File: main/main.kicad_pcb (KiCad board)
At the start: 4 copper layers, 94.8 x 88 mm, 101 parts, among them J1 Micro_SD_Card_Det1, J10 STKHEADER_B1_R, J11 STKHEADER_B1_L, J12 STKHEADER_B2_R, J13 SCRTERM_Board3ConnPt, J2 HEADER_ST-Link IN, J4 3.7V_IN, J5 Voltmeter_OUT, J6 SCRTERM_Board3ConnPt, J7 HEADER_ST-Link IN, J8 HEADER_ST-Link IN, J9 STKHEADER_B2_L, U1 STM32F405RGTx, U12 BMI323, U13 MAX-M10S, U2 LSM6DSL, U3 MMC5883MA, U4 AP63203WU, U5 THVD1420D, U7 STM32G071CBT6, U8 STM32G071CBT6, U9 THVD1420D

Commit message: work on dsn checklist
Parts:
- removed C22, C31, C33: 100n, Capacitor_SMD:C_0603_1608Metric
- added Q1: AO3401A, Package_TO_SOT_SMD:SOT-23, F.Cu at (176.9, 53.1)
- added R18: 10k, Resistor_SMD:R_0603_1608Metric, F.Cu at (173.4, 52.3)
- J4: value 3.7V_IN -> 7.4IN
- L1: footprint Inductor_SMD:L_0603_1608Metric -> Inductor_SMD:L_6.3x6.3_H3
- U10, U11, U6: footprint Oscillator:Oscillator_SMD_SCTF_SX3M8.000M20F30TNN -> Crystal:Crystal_SMD_3225-4Pin_3.2x2.5mm
- U5, U9: value THVD1420D -> SP3485EN
- moved L1 4.14 mm to (173.8, 63.0)
- moved R14 2.19 mm to (192.7, 116.3), turned to 90 degrees
- moved D1 1.86 mm to (173.3, 83.3)
- moved R8 1.80 mm to (171.6, 83.3), turned to -90 degrees
- moved D2 1.44 mm to (190.9, 116.3)
- moved U10 1.10 mm to (131.6, 127.6), turned to 180 degrees
- moved U6 0.36 mm to (178.9, 70.5), turned to 90 degrees
- moved R15 0.30 mm to (143.4, 116.3), turned to 0 degrees
- moved U11 0.26 mm to (189.3, 126.5), turned to 180 degrees
- moved D3 0.07 mm to (143.5, 118.0)
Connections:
- AE1 pad 2: (no net) -> GND
- C16 pad 1: /Board1/BAT_+ -> Net-(Q1-S)
- C35 pad 1: /Board2/B_VDDIO -> +3V3
- D1 pad 1: GND -> Net-(D1-K)
- D2 pad 1: GND -> Net-(D2-K)
- D3 pad 1: GND -> Net-(D3-K)
- R14 pad 2: /B2_USR_LED -> Net-(D2-K)
- R15 pad 2: /B3_USR_LED -> Net-(D3-K)
- R8 pad 2: /B1_USR_LED -> Net-(D1-K)
- U1 pad 6: unconnected-(U1-PH1-Pad6) -> /B1_OSC_OUT
- U10 pad 1: unconnected-(U10-OE-Pad1) -> /B3_OSC_OUT
- U10 pad 4: +3V3 -> GND
- U11 pad 1: unconnected-(U11-OE-Pad1) -> /B2_OSC_OUT
- U11 pad 4: +3V3 -> GND
- U12 pad 5: /Board2/B_VDDIO -> +3V3
- U4 pad 2: /Board1/BAT_+ -> Net-(Q1-S)
- U4 pad 3: /Board1/BAT_+ -> Net-(Q1-S)
- U6 pad 1: unconnected-(U6-OE-Pad1) -> /B1_OSC_OUT
- U6 pad 4: +3V3 -> GND
- U7 pad 9: unconnected-(U7A-PF1-OSC_OUT-Pad9) -> /B2_OSC_OUT
- U8 pad 9: unconnected-(U8A-PF1-OSC_OUT-Pad9) -> /B3_OSC_OUT
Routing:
- net /Board1/BAT_+: track 27.9 -> 23.0 mm
- net Net-(U4-SW): track 5.17 -> 9.76 mm
- net Net-(Q1-S): track 0.00 -> 4.26 mm
- net /B3_OSC_IN: track 3.01 -> 6.99 mm
- net GND: track 22.4 -> 18.7 mm, vias 184 -> 242
- net /B3_OSC_OUT: track 0.00 -> 3.74 mm
- net /B3_USR_LED: track 6.84 -> 3.19 mm
- net /B2_OSC_IN: track 3.07 -> 6.34 mm
- net /B1_OSC_IN: track 1.94 -> 4.85 mm
- net /B2_OSC_OUT: track 0.00 -> 2.78 mm
- net /Board2/B_VDDIO: track 2.72 -> 0.00 mm, vias 1 -> 0
- net /B1_OSC_OUT: track 0.00 -> 2.45 mm
- net /B2_USR_LED: track 6.41 -> 4.41 mm
- net Net-(D2-K): track 0.00 -> 1.81 mm
- net Net-(D3-K): track 0.00 -> 1.80 mm
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- added copper zone on F.Cu, net Net-(Q1-S)
- removed copper zone on F.Cu, net /Board1/BAT_+

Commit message: continue fixing chklst
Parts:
- added C22: 100n, Capacitor_SMD:C_0603_1608Metric, F.Cu at (167.8, 81.1)
- added C23: 100n, Capacitor_SMD:C_0603_1608Metric, F.Cu at (210.7, 114.5)
- added C31: 100n, Capacitor_SMD:C_0603_1608Metric, F.Cu at (144.5, 126.7)
- added R19: 10k, Resistor_SMD:R_0603_1608Metric, F.Cu at (174.2, 71.8)
- added R20: 10k, Resistor_SMD:R_0603_1608Metric, F.Cu at (205.0, 77.1)
- added R21: 22, Resistor_SMD:R_0603_1608Metric, F.Cu at (188.6, 81.7)
- added R22: 22, Resistor_SMD:R_0603_1608Metric, F.Cu at (186.0, 81.6)
- added R23: 22, Resistor_SMD:R_0603_1608Metric, F.Cu at (197.2, 116.3)
- added RN1: R_Net04_10k, Resistor_SMD:R_Array_Convex_4x0603, F.Cu at (197.2, 64.7)
- J4: value 7.4IN -> 7.4V_IN
- moved AE1 0.44 mm to (137.4, 97.6)
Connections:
- J1 pad SH: unconnected-(J1-SHIELD-PadSH)_3 -> GND
- J9 pad 3: /B_MISO -> /B_MOSI
- J9 pad 4: /B_MOSI -> /B_MISO
- U1 pad 21: /B2_CLK -> Net-(U1-PA5)
- U1 pad 23: /B2_MOSI -> Net-(U1-PA7)
- U1 pad 60: unconnected-(U1-BOOT0-Pad60) -> Net-(U1-BOOT0)
- U13 pad 18: /GPS_SAFEBOOT -> unconnected-(U13-~{SAFEBOOT}-Pad18)
- U7 pad 43: /B_MISO -> Net-(U7A-PB4)
- U8 pad 2: /GPS_SAFEBOOT -> unconnected-(U8A-PC14-OSC32_IN-Pad2)
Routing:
- net /GPS_SAFEBOOT: track 21.8 -> 0.00 mm, vias 2 -> 0
- net Net-(U1-BOOT0): track 0.00 -> 16.2 mm, vias 0 -> 2
- net /SDIO_D2: track 18.0 -> 30.6 mm, vias 2 -> 3
- net /SDIO_D3: track 17.8 -> 29.1 mm, vias 2 -> 3
- net /SDIO_D0: track 14.6 -> 25.1 mm, vias 0 -> 2
- net /SDIO_CMD: track 19.8 -> 28.3 mm
- net /B1_NRST: track 22.7 -> 29.6 mm
- net /SDIO_D1: track 14.9 -> 20.5 mm
- net /B2_CLK: track 12.3 -> 7.29 mm
- net /B2_MOSI: track 7.74 -> 3.19 mm
- net +3V3: track 143.3 -> 147.2 mm, vias 34 -> 37
- net Net-(U1-PA7): track 0.00 -> 3.09 mm
- net /B2_NRST: track 22.6 -> 25.5 mm, vias 1 -> 2
- net Net-(U7A-PB4): track 0.00 -> 2.65 mm
- net Net-(U1-PA5): track 0.00 -> 2.24 mm
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
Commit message: prep gerber and cpl/bom
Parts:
- added C47: 10p, Capacitor_SMD:C_0603_1608Metric, F.Cu at (176.4, 68.5)
- added C48: 10p, Capacitor_SMD:C_0603_1608Metric, F.Cu at (178.5, 73.4)
- added C49: 10p, Capacitor_SMD:C_0603_1608Metric, F.Cu at (184.8, 126.5)
- added C50: 10p, Capacitor_SMD:C_0603_1608Metric, F.Cu at (190.6, 126.4)
- added C51: 10p, Capacitor_SMD:C_0603_1608Metric, F.Cu at (131.4, 130.1)
- added C52: 10p, Capacitor_SMD:C_0603_1608Metric, F.Cu at (134.4, 128.3)
- added FID1: Fiducial, Fiducial:Fiducial_1mm_Mask2mm, F.Cu at (130.0, 47.4)
- added FID2: Fiducial, Fiducial:Fiducial_1mm_Mask2mm, F.Cu at (200.8, 47.4)
- added FID3: Fiducial, Fiducial:Fiducial_1mm_Mask2mm, F.Cu at (130.0, 142.6)
- added MB1: R-B1a, Panel:MouseBite, F.Cu at (166.5, 51.1)
- added MB10: B3-B2a, Panel:MouseBite, F.Cu at (157.9, 103.5)
- added MB11: B3-B2b, Panel:MouseBite, F.Cu at (157.9, 127.0)
- added MB12: F-B3a, Panel:MouseBite, F.Cu at (124.5, 95.2)
- added MB13: F-B3b, Panel:MouseBite, F.Cu at (150.0, 95.2)
- added MB14: B3-Fa, Panel:MouseBite, F.Cu at (131.0, 133.8)
- added MB15: B3-Fb, Panel:MouseBite, F.Cu at (152.0, 133.8)
- added MB2: R-B1b, Panel:MouseBite, F.Cu at (203.5, 51.1)
- added MB3: F-B1a, Panel:MouseBite, F.Cu at (158.9, 63.0)
- added MB4: F-B1b, Panel:MouseBite, F.Cu at (158.9, 85.0)
- added MB5: B1-B2a, Panel:MouseBite, F.Cu at (168.5, 95.0)
- added MB6: B1-B2b, Panel:MouseBite, F.Cu at (185.5, 95.0)
- added MB7: B1-B2c, Panel:MouseBite, F.Cu at (203.0, 95.0)
- added MB8: B2-Ra, Panel:MouseBite, F.Cu at (170.0, 138.8)
- added MB9: B2-Rb, Panel:MouseBite, F.Cu at (201.0, 138.8)
- added TH1: Tooling, Panel:ToolingHole_1.152mm, F.Cu at (123.0, 47.4)
- added TH2: Tooling, Panel:ToolingHole_1.152mm, F.Cu at (207.8, 47.4)
- added TH3: Tooling, Panel:ToolingHole_1.152mm, F.Cu at (123.0, 142.6)
- added TH4: Tooling, Panel:ToolingHole_1.152mm, F.Cu at (207.8, 142.6)
- added TP1: GPS_SAFEBOOT, TestPoint:TestPoint_Pad_D1.0mm, F.Cu at (119.6, 112.9)
- added TP4: GND, TestPoint:TestPoint_Pad_D1.0mm, F.Cu at (119.6, 110.8)
- C16: value 10u -> 10u 25V; footprint Capacitor_SMD:C_0603_1608Metric -> Capacitor_SMD:C_0805_2012Metric
- D1, D2, D3: value LED -> LED red
- J12, J9: footprint Connector_PinHeader_2.54mm:PinHeader_1x08_P2.54mm_Vertical -> Connector_PinSocket_2.54mm:PinSocket_1x08_P2.54mm_Vertical
- L2: footprint Inductor_SMD:L_0402_1005Metric -> Inductor_SMD:L_0603_1608Metric
- R14, R15, R8: value 10k -> 1k
- R6, R7: value 4.7k -> 2.7k
- RN1: value R_Net04_10k -> 10k
- U10, U11, U6: value ~ -> 16MHz
- U3: value MMC5883MA -> MMC5983MA
- moved R1 5.32 mm to (199.4, 56.4), turned to 90 degrees
- moved U11 1.60 mm to (187.7, 126.5)
- moved C28 1.07 mm to (198.0, 72.8)
- moved RN1 0.81 mm to (197.1, 63.9), turned to 0 degrees
- moved C16 0.50 mm to (177.5, 55.8)
- moved L1 0.30 mm to (173.8, 63.3)
- moved C18 0.27 mm to (177.3, 57.6)
- moved C21 0.27 mm to (177.3, 59.1)
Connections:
- RN1 pad 2: /SDIO_D3 -> +3V3
- RN1 pad 3: /SDIO_D2 -> +3V3
- RN1 pad 4: /SDIO_D1 -> +3V3
- RN1 pad 5: /SDIO_D0 -> /SDIO_D3
- RN1 pad 6: (no net) -> /SDIO_D2
- RN1 pad 7: (no net) -> /SDIO_D1
- RN1 pad 8: (no net) -> /SDIO_D0
- U13 pad 18: unconnected-(U13-~{SAFEBOOT}-Pad18) -> /Board3/GPS_SAFEBOOT
- U3 pad 4: unconnected-(U3-NC-Pad4) -> +3V3
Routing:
- net GND: track 18.4 -> 22.3 mm, vias 248 -> 249
- net /B2_OSC_IN: track 6.34 -> 9.79 mm
- net +3V3: track 147.2 -> 149.9 mm, vias 37 -> 39
- net /Board3/GPS_SAFEBOOT: track 0.00 -> 2.66 mm
- net /B3_OSC_OUT: track 3.74 -> 6.04 mm
- net /SDIO_D0: track 25.1 -> 22.9 mm
- net /B1_OSC_OUT: track 2.45 -> 4.45 mm
- net /B1_RS485_TX: track 21.3 -> 19.6 mm
- net /B3_OSC_IN: track 6.99 -> 8.71 mm
- net /B1_OSC_IN: track 4.85 -> 6.54 mm
- net /B2_OSC_OUT: track 2.78 -> 4.45 mm
- net Net-(J5-Pin_2): track 6.24 -> 7.89 mm
- net /Mag_SCL: track 8.34 -> 9.11 mm
- net /B1_USR_LED: track 14.8 -> 14.0 mm
- net /MAG_INT: track 17.8 -> 17.1 mm
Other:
- board size 94.8 x 88 mm -> 94.8 x 99.2 mm
- board text added: "CTRL-F PAYLOAD 2026 B1 / B2 / B3 PANEL"
- board text added: "JLCJLCJLCJLC"

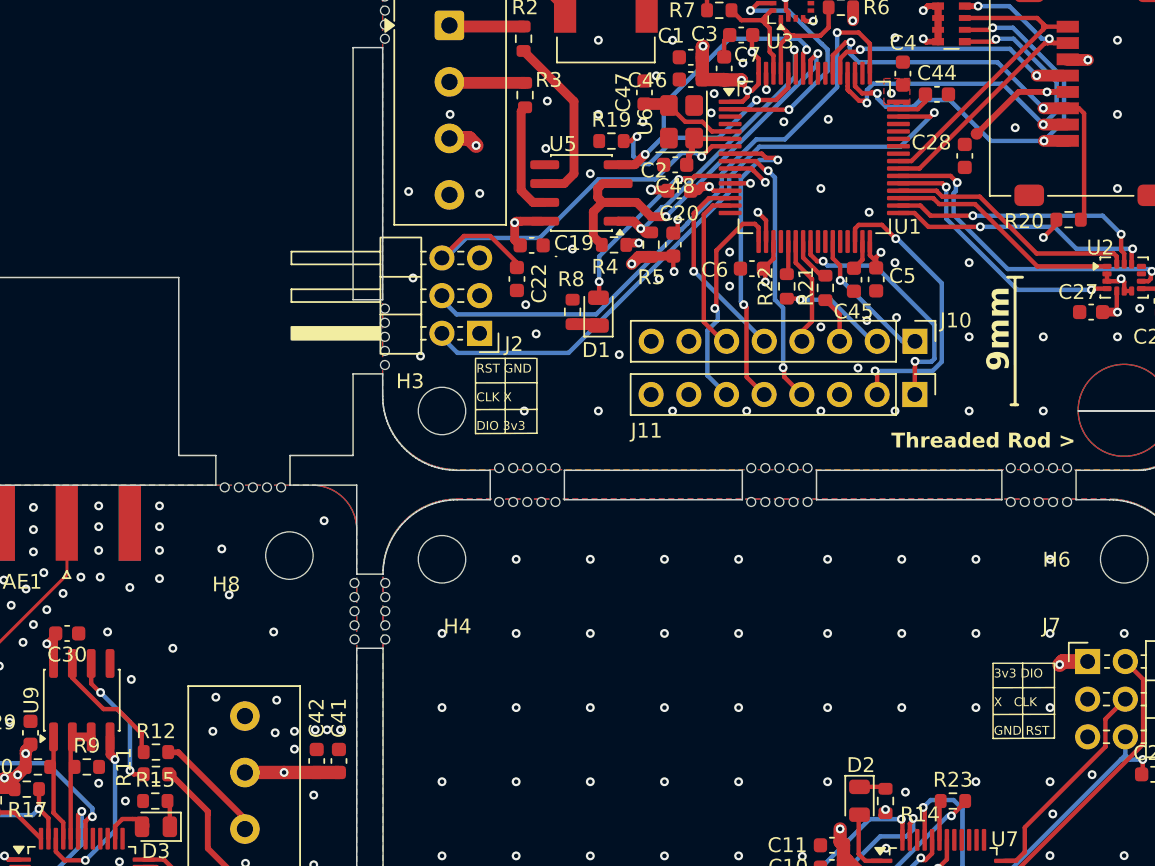
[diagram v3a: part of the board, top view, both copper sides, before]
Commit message: add doc and move SD card VCAP to fit
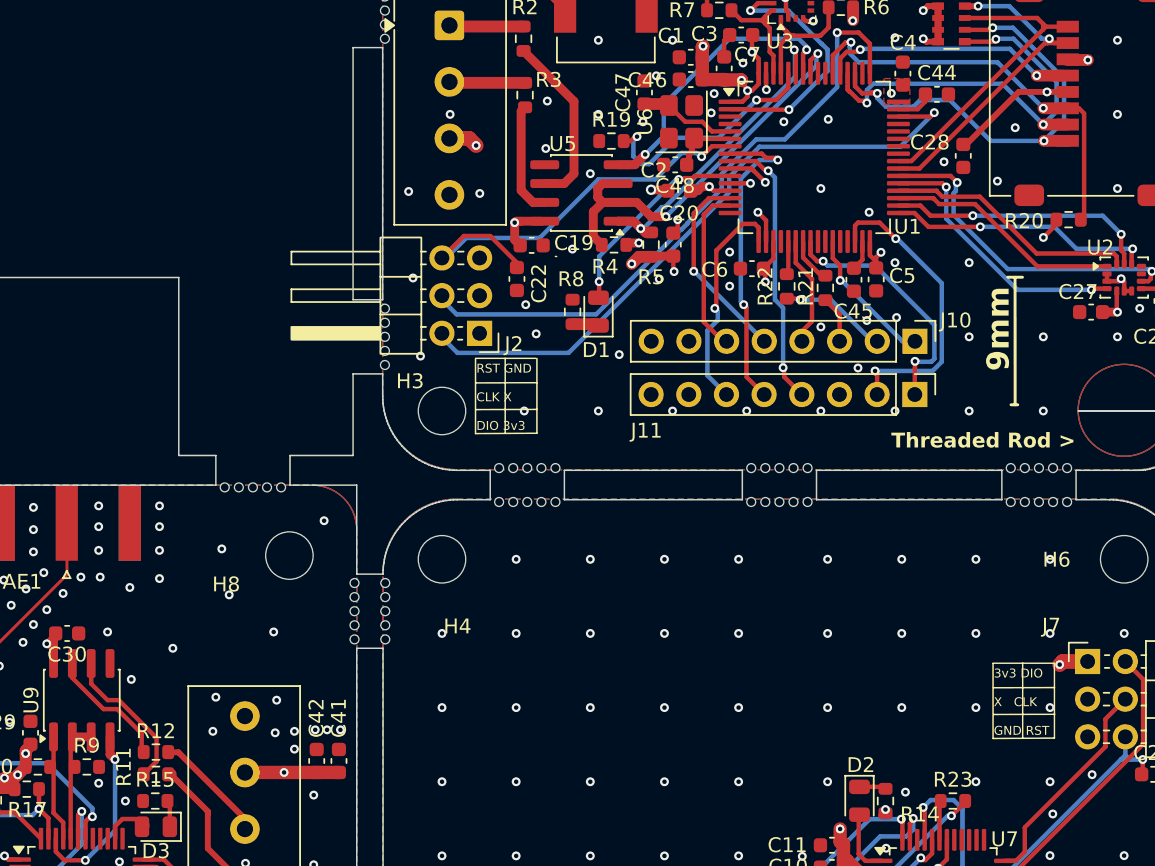
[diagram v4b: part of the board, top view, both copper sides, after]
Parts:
- moved C28 0.10 mm to (197.9, 72.8)
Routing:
- net +3V3: track 149.9 -> 151.0 mm
- net Net-(U9-A): track 9.36 -> 10.1 mm, vias 2 -> 0
- net GND: vias 249 -> 251
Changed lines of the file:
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@@
 	(footprint "Capacitor_SMD:C_0603_1608Metric"
 		(layer "F.Cu")
-		(at 198 72.8 -90)
+		(at 197.9 72.8 -90)
 		(descr "Capacitor SMD 0603 (1608 Metric), square (rectangular) end terminal, IPC-7351 nominal, (Body size source: IPC-SM-782 page 76, https://www.pcb-3d.com/wordpress/wp-content/uploads/ipc-sm-782a_amendment_1_and_2.pdf)")
 		(tags "capacitor")
@@
 	)
 	(via
+		(at 200.2 74.5)
+		(size 0.6)
+		(drill 0.3)
+		(layers "F.Cu" "B.Cu")
+		(free yes)
+		(net "GND")
+	)
+	(via
 		(at 188.295 90)
 		(size 0.6)
@@
 	)
 	(via
+		(at 196.6 73.2)
+		(size 0.6)
+		(drill 0.3)
+		(layers "F.Cu" "B.Cu")
+		(free yes)
+		(net "GND")
+	)
+	(via
 		(at 198.295 55)
 		(size 0.6)
@@
 	)
 	(segment
-		(start 139.69288 108.98288)
-		(end 139.095 108.385)
+		(start 140.957106 109.5)
+		(end 143.5 112.042894)
 		(width 0.3)
 		(layer "F.Cu")
@@
 	)
 	(segment
-		(start 141.96 114.5)
-		(end 141.71 114.25)
+		(start 139.095 107.025)
+		(end 139.095 108.395)
 		(width 0.3)
 		(layer "F.Cu")
@@
 	)
 	(segment
-		(start 139.095 108.385)
-		(end 139.095 107.025)
+		(start 140.2 109.5)
+		(end 140.957106 109.5)
 		(width 0.3)
 		(layer "F.Cu")
@@
 	)
 	(segment
-		(start 142.635 114.5)
-		(end 141.96 114.5)
+		(start 143.5 112.042894)
+		(end 143.5 113.635)
 		(width 0.3)
 		(layer "F.Cu")
@@
 	)
 	(segment
-		(start 139.72712 108.98288)
-		(end 139.69288 108.98288)
+		(start 139.095 108.395)
+		(end 140.2 109.5)
 		(width 0.3)
 		(layer "F.Cu")
 		(net "Net-(U9-A)")
 	)
-	(via
-		(at 141.71 114.25)
-		(size 0.6)
-		(drill 0.3)
-		(layers "F.Cu" "B.Cu")
-		(net "Net-(U9-A)")
-	)
-	(via
-		(at 139.72712 108.98288)
-		(size 0.6)
-		(drill 0.3)
-		(layers "F.Cu" "B.Cu")
-		(net "Net-(U9-A)")
-	)
-	(segment
-		(start 141.71 110.96576)
-		(end 139.72712 108.98288)
-		(width 0.3)
-		(layer "B.Cu")
-		(net "Net-(U9-A)")
-	)
 	(segment
-		(start 141.71 114.25)
-		(end 141.71 110.96576)
+		(start 143.5 113.635)
+		(end 142.635 114.5)
 		(width 0.3)
-		(layer "B.Cu")
+		(layer "F.Cu")
 		(net "Net-(U9-A)")
 	)
@@
 	)
 	(segment
-		(start 198.82 71.3075)
-		(end 198.795 71.3075)
-		(width 0.8)
+		(start 198.1025 72.025)
+		(end 198 72.025)
+		(width 0.4)
 		(layer "F.Cu")
 		(net "+3V3")
@@
 	)
 	(segment
-		(start 199.61375 70.51375)
-		(end 198.82 71.3075)
-		(width 0.4)
-		(layer "F.Cu")
-		(net "+3V3")
-	)
-	(segment
 		(start 180.75 74.85)
 		(end 180.3 74.85)
@@
 	)
 	(segment
-		(start 201.64 68.4875)
-		(end 204.65 68.4875)
-		(width 0.4)
-		(layer "F.Cu")
-		(net "+3V3")
-	)
-	(segment
 		(start 133.25 114.75)
 		(end 133.25 114.825)
@@
 	)
 	(segment
+		(start 204.65 68.4875)
+		(end 201.64 68.4875)
+		(width 0.4)
+		(layer "F.Cu")
+		(net "+3V3")
+	)
+	(segment
 		(start 176.2875 57.3625)
 		(end 176.525 57.6)
@@
 	)
 	(segment
+		(start 201.64 68.4875)
+		(end 198.1025 72.025)
+		(width 0.4)
+		(layer "F.Cu")
+		(net "+3V3")
+	)
+	(segment
 		(start 167.65 78.4625)
 		(end 168.02 78.8325)
@@
 	)
 	(segment
-		(start 199.61375 70.51375)
-		(end 201.64 68.4875)
-		(width 0.4)
-		(layer "F.Cu")
-		(net "+3V3")
-	)
-	(segment
 		(start 183.35 68.4)
 		(end 183.35 68.8)
@@
 	)
 	(segment
-		(start 190.6 78.575)
-		(end 190.6 77.69688)
+		(start 190.6 77.5)
+		(end 190.8 77.3)
 		(width 0.3)
 		(layer "F.Cu")
@@
 	)
 	(segment
-		(start 190.84688 77.45)
-		(end 192.4125 77.45)
+		(start 198.795 129.275394)
+		(end 195.380394 132.69)
 		(width 0.3)
 		(layer "F.Cu")
@@
 	)
 	(segment
-		(start 198.795 129.275394)
-		(end 195.380394 132.69)
+		(start 193.29 132.69)
+		(end 192.09 133.89)
 		(width 0.3)
 		(layer "F.Cu")
@@
 	)
 	(segment
-		(start 190.6 77.69688)
-		(end 190.84688 77.45)
+		(start 191.95 87.3)
+		(end 191.85 87.2)
 		(width 0.3)
 		(layer "F.Cu")
@@
 	)
 	(segment
-		(start 193.29 132.69)
-		(end 192.09 133.89)
+		(start 195.380394 132.69)
+		(end 193.29 132.69)
 		(width 0.3)
 		(layer "F.Cu")
@@
 	)
 	(segment
-		(start 191.95 87.3)
-		(end 191.85 87.2)
+		(start 198.795 128.08562)
+		(end 198.795 129.275394)
 		(width 0.3)
 		(layer "F.Cu")
@@
 	)
 	(segment
-		(start 192.4125 77.45)
-		(end 193.345 78.3825)
+		(start 190.8 77.3)
+		(end 192.2625 77.3)
 		(width 0.3)
 		(layer "F.Cu")
@@
 	)
 	(segment
-		(start 195.380394 132.69)
-		(end 193.29 132.69)
+		(start 198.795 127.245)
+		(end 198.795 128.08562)
 		(width 0.3)
 		(layer "F.Cu")
@@
 	)
 	(segment
-		(start 198.795 128.08562)
-		(end 198.795 129.275394)
+		(start 190.6 78.575)
+		(end 190.6 77.5)
 		(width 0.3)
 		(layer "F.Cu")
@@
 	)
 	(segment
-		(start 198.795 127.245)
-		(end 198.795 128.08562)
+		(start 192.2625 77.3)
+		(end 193.345 78.3825)
 		(width 0.3)
 		(layer "F.Cu")
